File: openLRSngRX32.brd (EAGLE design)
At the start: 43 x 39.6 mm, 50 parts, among them IC1 STM32F10XCXT6, IC2 REG1117, U1 MPU-6000QFN-24

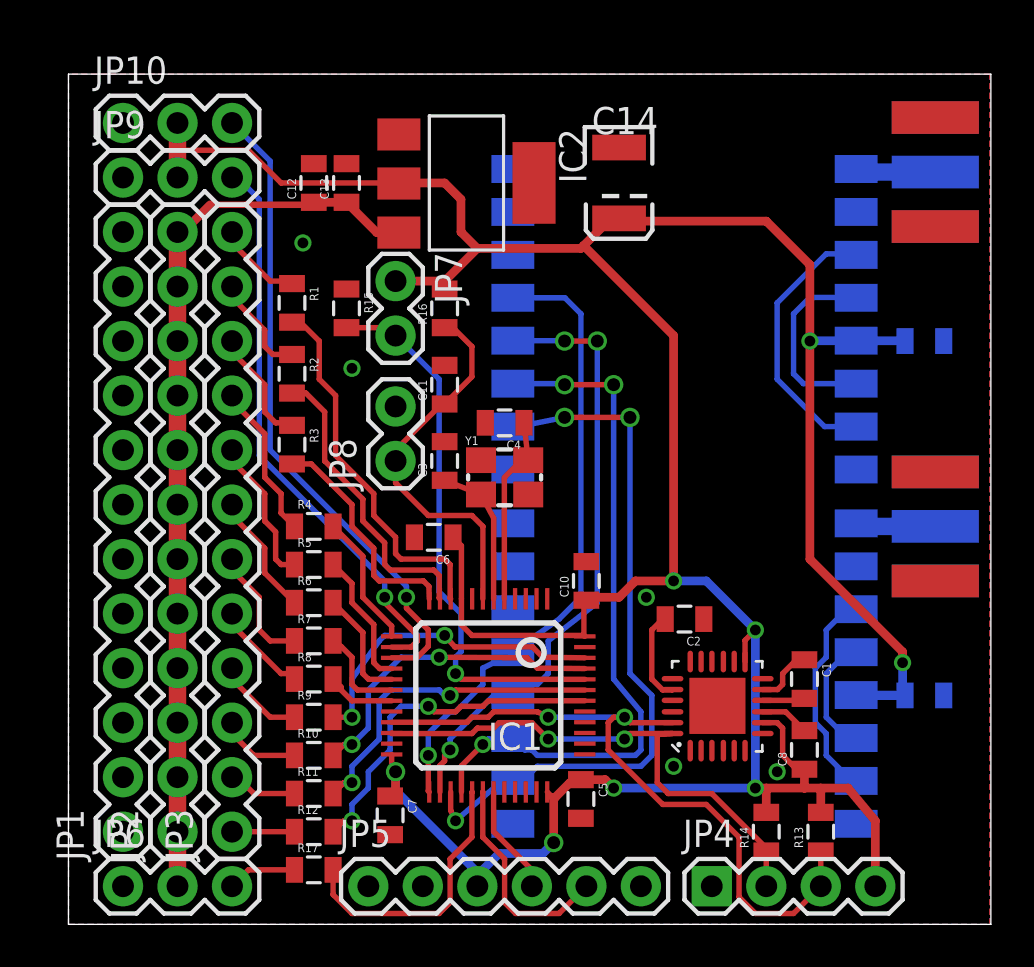
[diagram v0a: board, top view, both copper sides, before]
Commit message: more cs lines
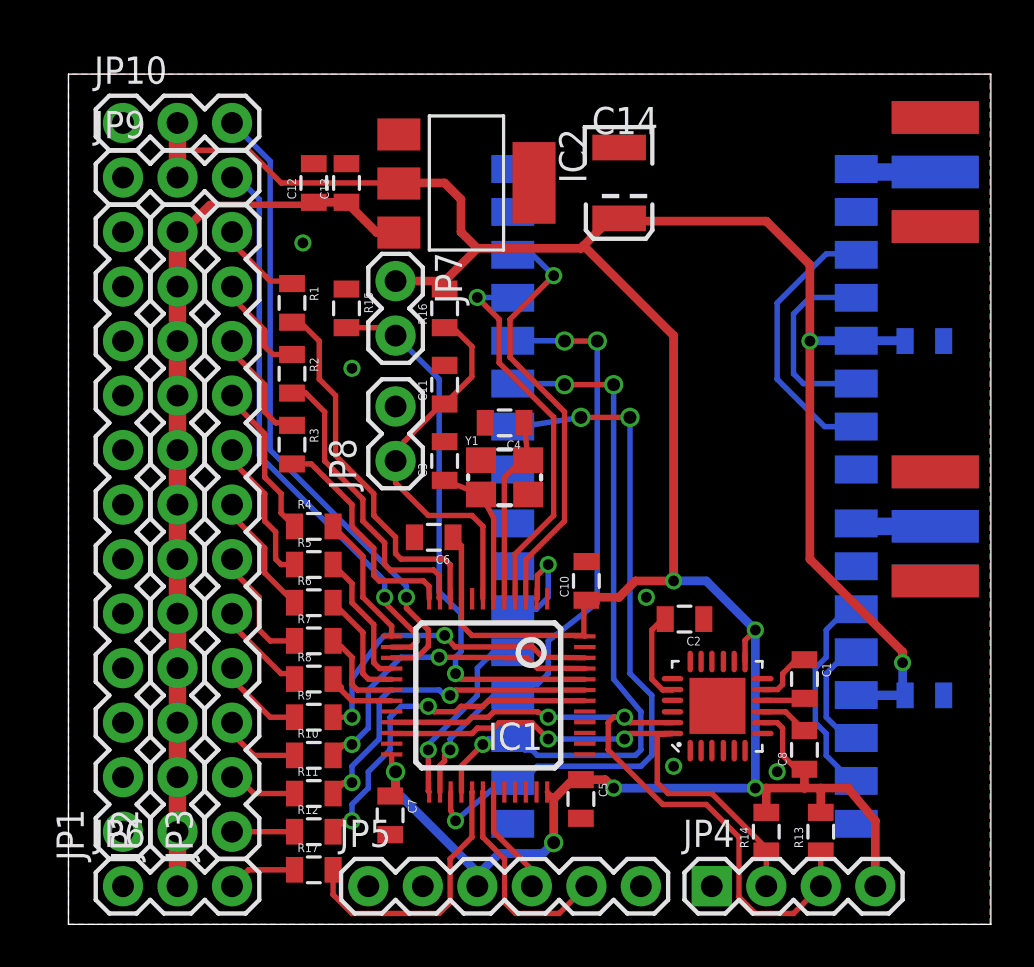
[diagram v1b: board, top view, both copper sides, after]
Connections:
- removed net N$21: U$1.14
- removed net N$22: U$2.14
- removed net NSS: IC1.25, U$1.13, U$2.13
- new net RFM1CS: IC1.25, U$1.13
- new net RFM1IRQ: IC1.2, U$1.14
- new net RFM2CS: IC1.4, U$2.13
- new net RFM2IRQ: IC1.3, U$2.14
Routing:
- net NSS: track 29.4 -> 0.00 mm, vias 1 -> 0
- net RFM2IRQ: track 0.00 -> 20.0 mm, vias 0 -> 1
- net RFM2CS: track 0.00 -> 17.9 mm, vias 0 -> 1
- net RFM1CS: track 0.00 -> 8.70 mm, vias 0 -> 1
- net RFM1IRQ: track 0.00 -> 5.23 mm, vias 0 -> 1
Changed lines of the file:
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@@
 <wire x1="12.838" y1="4.826" x2="12.33" y2="4.318" width="0.254" layer="1"/>
-</signal>
-<signal name="NSS">
-<contactref element="U$1" pad="13"/>
-<contactref element="U$2" pad="13"/>
-<contactref element="IC1" pad="25"/>
-<wire x1="16.808" y1="6.168" x2="16.764" y2="6.212" width="0.254" layer="1"/>
-<wire x1="16.764" y1="6.212" x2="16.764" y2="7.874" width="0.254" layer="1"/>
-<via x="16.764" y="7.874" extent="1-16" drill="0.5"/>
-<wire x1="16.764" y1="7.874" x2="16.764" y2="8.89" width="0.254" layer="16"/>
-<wire x1="16.764" y1="8.89" x2="17.78" y2="9.906" width="0.254" layer="16"/>
-<wire x1="17.78" y1="9.906" x2="18.034" y2="9.906" width="0.254" layer="16"/>
-<wire x1="18.034" y1="9.906" x2="19.304" y2="11.176" width="0.254" layer="16"/>
-<wire x1="19.304" y1="11.176" x2="19.304" y2="11.938" width="0.254" layer="16"/>
-<wire x1="19.304" y1="11.938" x2="19.812" y2="12.192" width="0.254" layer="16"/>
-<wire x1="19.812" y1="12.192" x2="20.304" y2="12.684" width="0.254" layer="16"/>
-<wire x1="20.304" y1="12.684" x2="20.702" y2="12.684" width="0.254" layer="16"/>
-<wire x1="20.702" y1="29.194" x2="23.13" y2="29.194" width="0.254" layer="16"/>
-<wire x1="23.13" y1="29.194" x2="23.876" y2="28.448" width="0.254" layer="16"/>
-<wire x1="23.876" y1="28.448" x2="23.876" y2="15.24" width="0.254" layer="16"/>
-<wire x1="23.876" y1="15.24" x2="22.86" y2="14.224" width="0.254" layer="16"/>
-<wire x1="22.86" y1="14.224" x2="20.718" y2="12.7" width="0.254" layer="16"/>
-<wire x1="20.718" y1="12.7" x2="20.702" y2="12.684" width="0.4064" layer="16"/>
 </signal>
 <signal name="SCK">
@@
 <wire x1="20.702" y1="23.194" x2="20.654" y2="23.194" width="0.254" layer="16"/>
 <wire x1="20.654" y1="23.194" x2="20.574" y2="23.114" width="0.254" layer="16"/>
-<wire x1="20.574" y1="23.114" x2="23.114" y2="23.622" width="0.254" layer="16"/>
-<via x="23.114" y="23.622" extent="1-16" drill="0.6"/>
-<wire x1="23.114" y1="23.622" x2="26.162" y2="23.622" width="0.254" layer="1"/>
+<wire x1="20.574" y1="23.114" x2="23.876" y2="23.622" width="0.254" layer="16"/>
+<via x="23.876" y="23.622" extent="1-16" drill="0.6"/>
+<wire x1="23.876" y1="23.622" x2="26.162" y2="23.622" width="0.254" layer="1"/>
 <via x="26.162" y="23.622" extent="1-16" drill="0.6"/>
 <wire x1="26.162" y1="23.622" x2="26.162" y2="11.684" width="0.254" layer="16"/>
@@
 <wire x1="21.13" y1="7.112" x2="20.702" y2="6.684" width="0.254" layer="16"/>
 </signal>
-<signal name="N$21">
+<signal name="RFM1IRQ">
 <contactref element="U$1" pad="14"/>
-</signal>
-<signal name="N$22">
+<contactref element="IC1" pad="2"/>
+<wire x1="21.808" y1="15.168" x2="21.844" y2="15.204" width="0.254" layer="1"/>
+<wire x1="21.844" y1="15.204" x2="21.844" y2="16.256" width="0.254" layer="1"/>
+<wire x1="21.844" y1="16.256" x2="22.352" y2="16.764" width="0.254" layer="1"/>
+<via x="22.352" y="16.764" extent="1-16" drill="0.5"/>
+<wire x1="22.352" y1="16.764" x2="22.352" y2="15.24" width="0.254" layer="16"/>
+<wire x1="22.352" y1="15.24" x2="21.796" y2="14.684" width="0.254" layer="16"/>
+<wire x1="21.796" y1="14.684" x2="20.702" y2="14.684" width="0.254" layer="16"/>
+</signal>
+<signal name="RFM2IRQ">
 <contactref element="U$2" pad="14"/>
+<contactref element="IC1" pad="3"/>
+<wire x1="21.308" y1="15.168" x2="21.308" y2="16.99" width="0.254" layer="1"/>
+<wire x1="21.308" y1="16.99" x2="23.114" y2="18.796" width="0.254" layer="1"/>
+<wire x1="23.114" y1="18.796" x2="23.114" y2="23.876" width="0.254" layer="1"/>
+<wire x1="23.114" y1="23.876" x2="20.574" y2="26.416" width="0.254" layer="1"/>
+<wire x1="20.574" y1="26.416" x2="20.574" y2="28.194" width="0.254" layer="1"/>
+<wire x1="20.574" y1="28.194" x2="22.606" y2="30.226" width="0.254" layer="1"/>
+<via x="22.606" y="30.226" extent="1-16" drill="0.5"/>
+<wire x1="22.606" y1="30.226" x2="21.638" y2="31.194" width="0.254" layer="16"/>
+<wire x1="21.638" y1="31.194" x2="20.702" y2="31.194" width="0.254" layer="16"/>
 </signal>
 <signal name="SCL">
@@
 <wire x1="7.874" y1="34.798" x2="7.62" y2="34.798" width="0.254" layer="16"/>
 </signal>
+<signal name="RFM2CS">
+<contactref element="IC1" pad="4"/>
+<contactref element="U$2" pad="13"/>
+<wire x1="20.808" y1="15.168" x2="20.808" y2="17.252" width="0.254" layer="1"/>
+<wire x1="20.808" y1="17.252" x2="22.606" y2="19.05" width="0.254" layer="1"/>
+<wire x1="22.606" y1="19.05" x2="22.606" y2="23.622" width="0.254" layer="1"/>
+<wire x1="22.606" y1="23.622" x2="20.066" y2="26.162" width="0.254" layer="1"/>
+<wire x1="20.066" y1="26.162" x2="20.066" y2="28.194" width="0.254" layer="1"/>
+<wire x1="20.066" y1="28.194" x2="19.05" y2="29.21" width="0.254" layer="1"/>
+<via x="19.05" y="29.21" extent="1-16" drill="0.5"/>
+<wire x1="19.05" y1="29.21" x2="20.686" y2="29.21" width="0.254" layer="16"/>
+<wire x1="20.686" y1="29.21" x2="20.702" y2="29.194" width="0.254" layer="16"/>
+</signal>
+<signal name="RFM1CS">
+<contactref element="U$1" pad="13"/>
+<contactref element="IC1" pad="25"/>
+<wire x1="16.808" y1="6.168" x2="16.764" y2="6.212" width="0.254" layer="1"/>
+<wire x1="16.764" y1="6.212" x2="16.764" y2="8.128" width="0.254" layer="1"/>
+<via x="16.764" y="8.128" extent="1-16" drill="0.5"/>
+<wire x1="16.764" y1="8.128" x2="16.764" y2="8.382" width="0.254" layer="16"/>
+<wire x1="16.764" y1="8.382" x2="19.05" y2="10.668" width="0.254" layer="16"/>
+<wire x1="19.05" y1="10.668" x2="19.05" y2="11.938" width="0.254" layer="16"/>
+<wire x1="19.05" y1="11.938" x2="19.796" y2="12.684" width="0.254" layer="16"/>
+<wire x1="19.796" y1="12.684" x2="20.702" y2="12.684" width="0.254" layer="16"/>
+</signal>
 </signals>

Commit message: MPU interrupt GND reinforcement
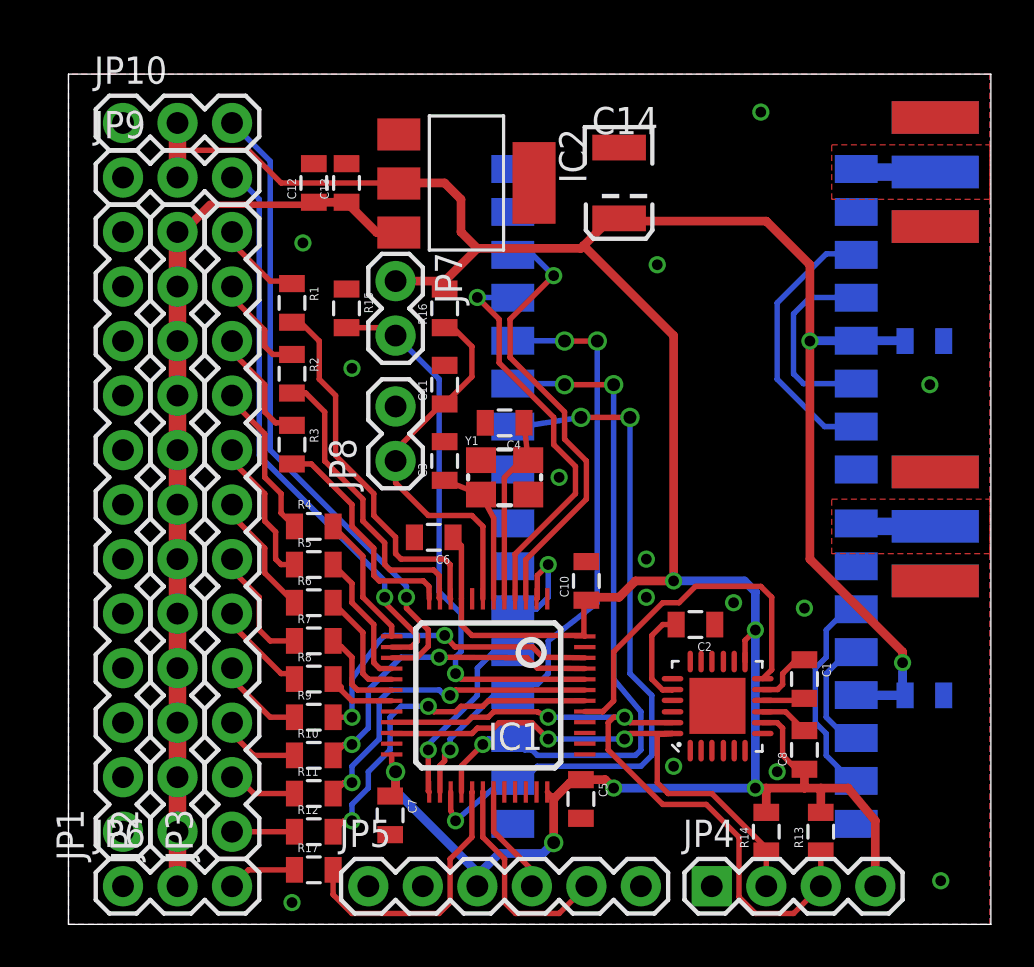
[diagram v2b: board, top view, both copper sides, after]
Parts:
- moved C2 0.57 mm to (29.2, 14.0)
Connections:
- net MPUINT: now also IC1.41
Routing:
- net MPUINT: track 0.00 -> 16.6 mm
- net 3V3: track 162.4 -> 163.4 mm
- net RFM2CS: track 17.9 -> 18.8 mm
- net RFM2IRQ: track 20.0 -> 20.8 mm
- net GND: vias 5 -> 14
- added copper zone on layer 1, net N$21
- added copper zone on layer 1, net N$22
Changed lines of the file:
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@@
 <element name="U1" library="SparkFun-Sensors" package="QFN-24-TESTING" value="MPU-6000QFN-24" x="30.226" y="10.16" rot="R90"/>
 <element name="C1" library="SparkFun-Capacitors" package="0805" value="" x="34.29" y="11.43" rot="R270"/>
-<element name="C2" library="SparkFun-Capacitors" package="0805" value="" x="28.702" y="14.224" rot="R180"/>
+<element name="C2" library="SparkFun-Capacitors" package="0805" value="" x="29.21" y="13.97" rot="R180"/>
 <element name="C3" library="SparkFun-Capacitors" package="0805" value="" x="17.526" y="21.59" rot="R90"/>
 <element name="C4" library="SparkFun-Capacitors" package="0805" value="" x="20.32" y="23.368" rot="R180"/>
@@
 <via x="13.208" y="25.908" extent="1-16" drill="0.5"/>
 <via x="26.924" y="15.24" extent="1-16" drill="0.5"/>
+<via x="30.988" y="14.986" extent="1-16" drill="0.5"/>
+<via x="26.924" y="17.018" extent="1-16" drill="0.5"/>
+<via x="22.86" y="20.828" extent="1-16" drill="0.5"/>
+<via x="34.29" y="14.732" extent="1-16" drill="0.5"/>
+<via x="40.132" y="25.146" extent="1-16" drill="0.5"/>
+<via x="40.64" y="2.032" extent="1-16" drill="0.5"/>
+<via x="32.258" y="37.846" extent="1-16" drill="0.5"/>
+<via x="27.432" y="30.734" extent="1-16" drill="0.5"/>
+<via x="10.414" y="1.016" extent="1-16" drill="0.5"/>
 </signal>
 <signal name="VCC">
@@
 <via x="32.004" y="13.716" extent="1-16" drill="0.5"/>
 <wire x1="32.004" y1="13.716" x2="32.004" y2="6.35" width="0.4064" layer="16"/>
-<wire x1="28.194" y1="16.002" x2="29.718" y2="16.002" width="0.4064" layer="16"/>
-<wire x1="29.718" y1="16.002" x2="32.004" y2="13.716" width="0.4064" layer="16"/>
+<wire x1="28.194" y1="16.002" x2="31.496" y2="16.002" width="0.4064" layer="16"/>
+<wire x1="31.496" y1="16.002" x2="32.004" y2="15.494" width="0.4064" layer="16"/>
+<wire x1="32.004" y1="15.494" x2="32.004" y2="13.716" width="0.4064" layer="16"/>
 <wire x1="24.014" y1="13.462" x2="24.014" y2="14.986" width="0.254" layer="1"/>
 <wire x1="24.014" y1="14.986" x2="24.13" y2="15.102" width="0.254" layer="1"/>
@@
 <contactref element="IC1" pad="3"/>
 <wire x1="21.308" y1="15.168" x2="21.308" y2="16.99" width="0.254" layer="1"/>
-<wire x1="21.308" y1="16.99" x2="23.114" y2="18.796" width="0.254" layer="1"/>
-<wire x1="23.114" y1="18.796" x2="23.114" y2="23.876" width="0.254" layer="1"/>
+<wire x1="21.308" y1="16.99" x2="24.13" y2="19.812" width="0.254" layer="1"/>
+<wire x1="24.13" y1="19.812" x2="24.13" y2="21.59" width="0.254" layer="1"/>
+<wire x1="24.13" y1="21.59" x2="23.114" y2="22.606" width="0.254" layer="1"/>
+<wire x1="23.114" y1="22.606" x2="23.114" y2="23.876" width="0.254" layer="1"/>
 <wire x1="23.114" y1="23.876" x2="20.574" y2="26.416" width="0.254" layer="1"/>
 <wire x1="20.574" y1="26.416" x2="20.574" y2="28.194" width="0.254" layer="1"/>
@@
 <wire x1="28.1268" y1="10.922" x2="27.686" y2="10.922" width="0.254" layer="1"/>
 <wire x1="27.686" y1="10.922" x2="27.178" y2="11.43" width="0.254" layer="1"/>
-<wire x1="27.178" y1="11.43" x2="27.178" y2="13.716" width="0.254" layer="1"/>
-<wire x1="27.178" y1="13.716" x2="27.686" y2="14.224" width="0.254" layer="1"/>
-<wire x1="27.686" y1="14.224" x2="27.802" y2="14.224" width="0.254" layer="1"/>
+<wire x1="27.178" y1="11.43" x2="27.178" y2="13.462" width="0.254" layer="1"/>
+<wire x1="27.178" y1="13.462" x2="27.686" y2="13.97" width="0.254" layer="1"/>
+<wire x1="27.686" y1="13.97" x2="28.31" y2="13.97" width="0.254" layer="1"/>
 </signal>
 <signal name="MPUINT">
 <contactref element="U1" pad="12"/>
+<contactref element="IC1" pad="41"/>
+<wire x1="32.3476" y1="11.4467" x2="32.766" y2="11.8651" width="0.254" layer="1"/>
+<wire x1="32.766" y1="11.8651" x2="32.766" y2="15.24" width="0.254" layer="1"/>
+<wire x1="32.766" y1="15.24" x2="32.258" y2="15.748" width="0.254" layer="1"/>
+<wire x1="32.258" y1="15.748" x2="29.21" y2="15.748" width="0.254" layer="1"/>
+<wire x1="29.21" y1="15.748" x2="28.448" y2="14.986" width="0.254" layer="1"/>
+<wire x1="28.448" y1="14.986" x2="27.686" y2="14.986" width="0.254" layer="1"/>
+<wire x1="27.686" y1="14.986" x2="25.4" y2="12.7" width="0.254" layer="1"/>
+<wire x1="25.4" y1="12.7" x2="25.4" y2="10.414" width="0.254" layer="1"/>
+<wire x1="25.4" y1="10.414" x2="24.892" y2="9.906" width="0.254" layer="1"/>
+<wire x1="24.892" y1="9.906" x2="24.88" y2="9.918" width="0.254" layer="1"/>
+<wire x1="24.88" y1="9.918" x2="24.058" y2="9.918" width="0.254" layer="1"/>
 </signal>
 <signal name="N$16">
@@
 <contactref element="U$2" pad="13"/>
 <wire x1="20.808" y1="15.168" x2="20.808" y2="17.252" width="0.254" layer="1"/>
-<wire x1="20.808" y1="17.252" x2="22.606" y2="19.05" width="0.254" layer="1"/>
-<wire x1="22.606" y1="19.05" x2="22.606" y2="23.622" width="0.254" layer="1"/>
+<wire x1="20.808" y1="17.252" x2="23.622" y2="20.066" width="0.254" layer="1"/>
+<wire x1="23.622" y1="20.066" x2="23.622" y2="21.336" width="0.254" layer="1"/>
+<wire x1="23.622" y1="21.336" x2="22.606" y2="22.352" width="0.254" layer="1"/>
+<wire x1="22.606" y1="22.352" x2="22.606" y2="23.622" width="0.254" layer="1"/>
 <wire x1="22.606" y1="23.622" x2="20.066" y2="26.162" width="0.254" layer="1"/>
 <wire x1="20.066" y1="26.162" x2="20.066" y2="28.194" width="0.254" layer="1"/>
@@
 <wire x1="19.796" y1="12.684" x2="20.702" y2="12.684" width="0.254" layer="16"/>
 </signal>
+<signal name="N$21">
+<polygon width="0.254" layer="1" pour="cutout">
+<vertex x="35.56" y="36.322"/>
+<vertex x="42.926" y="36.322"/>
+<vertex x="42.926" y="33.782"/>
+<vertex x="35.56" y="33.782"/>
+</polygon>
+</signal>
+<signal name="N$22">
+<polygon width="0.254" layer="1" pour="cutout">
+<vertex x="35.56" y="19.812"/>
+<vertex x="42.926" y="19.812"/>
+<vertex x="42.926" y="17.272"/>
+<vertex x="35.56" y="17.272"/>
+</polygon>
+</signal>
 </signals>

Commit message: minor board tuning
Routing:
- added copper zone on layer 16, net N$26
- added copper zone on layer 16, net N$27
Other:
- board size 43 x 39.6 mm -> 43 x 39.4 mm

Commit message: Last fixes... I hope
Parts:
- added C16: 47uF, SparkFun-Capacitors:EIA3528
- added C17: (no value), SparkFun-Capacitors:0805
- added D1: (no value), diode:DO-214AC
- added JP11: (no value), SparkFun-Connectors:1X02
- added LED1, LED2: (no value), led:SML0805
- added R18, R19: 330R, SparkFun-Resistors:0805
- C1, C13: value (none) -> 100n
- C12: value (none) -> 1uF
- C2: value (none) -> 2n2
- C3, C4: value (none) -> 15p
- R1, R10, R11, R12, R15, R17, R2, R3, R4, R5, R6, R7, R8, R9: value (none) -> 1k
- R13, R14: value (none) -> 4k7
- R16: value (none) -> 10k
- Y1: value (none) -> 8MHz
- moved C12 8.90 mm to (20.3, 34.0), turned to 270 degrees
- moved IC2 7.38 mm to (25.9, 35.1), turned to 90 degrees
- moved C13 7.04 mm to (19.3, 37.6), turned to 180 degrees
- moved C14 6.90 mm to (32.5, 35.3)
- moved C5 1.37 mm to (25.1, 6.35), turned to 0 degrees
- moved C10 0.51 mm to (24.6, 16.0)
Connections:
- removed net DTR: JP5.6
- removed net VBAT: IC1.1
- new net N$28: C12.1, C13.1, C16.A, D1.C, IC2.3, JP11.2
- new net N$30: LED2.C, R19.2
- new net N$31: IC1.32, LED1.A
- new net N$32: IC1.37, LED2.A
- net 3V3: now also C17.1, IC1.1
- net GND: now also C16.C, C17.2, JP11.1, R18.1, R19.1, U$1.15, U$2.15
- net N$29: now also LED1.C, R18.2; no longer JP5.2
- net VCC: now also D1.A; no longer C12.1, C13.1, IC2.3
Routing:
- net N$28: track 0.00 -> 22.9 mm
- net N$29: track 0.00 -> 20.3 mm, vias 0 -> 2
- net N$30: track 0.00 -> 13.6 mm, vias 0 -> 2
- net 3V3: track 163.4 -> 171.0 mm, vias 8 -> 7
- net N$32: track 0.00 -> 5.38 mm
- net VCC: track 42.0 -> 45.8 mm
- net N$31: track 0.00 -> 3.77 mm
- net RFM2IRQ: track 20.8 -> 21.7 mm
- net GND: vias 14 -> 18

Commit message: cleanup
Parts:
- LED1: value (none) -> RED
- LED2: value (none) -> GREEN

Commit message: tuning still
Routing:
- net SCK: track 29.0 -> 28.6 mm, vias 3 -> 1
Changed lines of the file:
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@@
 <wire x1="19.812" y1="10.668" x2="20.686" y2="10.668" width="0.254" layer="16"/>
 <wire x1="20.686" y1="10.668" x2="20.702" y2="10.684" width="0.254" layer="16"/>
-<wire x1="20.702" y1="27.194" x2="23.098" y2="27.194" width="0.254" layer="16"/>
-<wire x1="23.098" y1="27.194" x2="23.114" y2="27.178" width="0.4064" layer="16"/>
-<via x="23.114" y="27.178" extent="1-16" drill="0.6"/>
-<wire x1="23.114" y1="27.178" x2="24.638" y2="27.178" width="0.254" layer="1"/>
-<via x="24.638" y="27.178" extent="1-16" drill="0.6"/>
-<wire x1="24.638" y1="27.178" x2="24.638" y2="14.986" width="0.254" layer="16"/>
+<wire x1="23.876" y1="27.194" x2="23.876" y2="27.178" width="0.254" layer="16"/>
+<wire x1="23.876" y1="27.178" x2="24.638" y2="26.416" width="0.254" layer="16"/>
+<wire x1="24.638" y1="26.416" x2="24.638" y2="14.986" width="0.254" layer="16"/>
 <wire x1="24.638" y1="14.986" x2="22.352" y2="13.208" width="0.254" layer="16"/>
 <wire x1="22.352" y1="13.208" x2="22.352" y2="11.684" width="0.254" layer="16"/>
@@
 <wire x1="21.59" y1="11.176" x2="20.718" y2="10.668" width="0.254" layer="16"/>
 <wire x1="20.718" y1="10.668" x2="20.702" y2="10.684" width="0.4064" layer="16"/>
+<wire x1="20.702" y1="27.194" x2="23.876" y2="27.194" width="0.254" layer="16"/>
 </signal>
 <signal name="MOSI">

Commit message: GB leds
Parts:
- added LED3: RED, led:SML0805
- added R20: 330R, SparkFun-Resistors:0805
- LED1: value RED -> GRN
- LED2: value GREEN -> BLU
- moved LED1 16.9 mm to (40.4, 7.87)
- moved R18 15.2 mm to (26.2, 4.32), turned to 180 degrees
- moved LED2 12.5 mm to (40.4, 5.59)
- moved R19 10.5 mm to (29.2, 4.32), turned to 180 degrees
- moved C5 0.51 mm to (24.6, 6.35), turned to 180 degrees
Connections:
- removed net N$29: LED1.C, R18.2
- new net N$33: IC1.32, R20.2
- new net N$34: IC1.33, R18.2
- new net N$35: IC1.34, R19.2
- net GND: now also LED1.C, LED2.C, LED3.C; no longer R18.1, R19.1
- net N$30: now also LED3.A, R20.1; no longer LED2.C, R19.2
- net N$31: now also R18.1; no longer IC1.32
- net N$32: now also R19.1; no longer IC1.37
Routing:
- net N$29: track 20.3 -> 0.00 mm, vias 2 -> 0
- net N$30: track 13.6 -> 28.2 mm
- net N$35: track 0.00 -> 11.2 mm
- net N$31: track 3.77 -> 15.0 mm, vias 0 -> 2
- net N$34: track 0.00 -> 7.80 mm
- net N$32: track 5.38 -> 11.3 mm, vias 0 -> 2
- net N$33: track 0.00 -> 2.91 mm
- net 3V3: track 171.0 -> 173.3 mm
- net SCL: track 32.8 -> 33.8 mm
- net SDA: track 24.7 -> 25.4 mm
- net GND: vias 18 -> 20
